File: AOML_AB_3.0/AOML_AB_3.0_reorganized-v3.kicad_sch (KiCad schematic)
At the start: 103 parts, among them IC11 SN74LVC1G3157DCKR, J1 Conn_01x04, J2 216550-1, J24 Conn_01x02, J3 Conn_01x03, J4 Conn_01x07, J5 Conn_01x03, J6 Conn_01x03, J7 Screw_Terminal_01x07, SW1 TS02-66-70-BK-160-LCR-D, U1 L7812ABD2T-TR, U2 LM7805MPX, U3 MCP1825ST-3302E/DB, U4 MAX3232, U5 INA213AIDCKR, U6 STM32F103RBTx, U7 AT24C01D-STUM-T, Y1 8MHz

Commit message: Board V3.0 rev3 completed: several footprints fixed, added mosfet inverter to GPS data input, buffer to Vin measurement, jumper to 12V motor supply bus, and made power rails wider
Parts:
- removed J6: Conn_01x03, Connector_PinHeader_2.54mm:PinHeader_1x03_P2.54mm_Vertical, symbol Connector_Generic:Conn_01x03
- removed JP10, JP11, JP9: SolderJumper_2_Open, Jumper:SolderJumper-2_P1.3mm_Open_RoundedPad1.0x1.5mm, symbol Jumper:SolderJumper_2_Open
- removed TP7: GND, TestPoint:TestPoint_Pad_1.0x1.0mm, symbol Connector:TestPoint
- added C78: 0.1u, Capacitor_01uF-0805:CAP_CL21_SAM, symbol Device:C
- added F1: 1A, Polyfuse_1A_1812:0ZCG_BEL, symbol Device:Polyfuse
- added J25: Conn_01x03, Connector_PinHeader_2.54mm:PinHeader_1x03_P2.54mm_Vertical, symbol Connector_Generic:Conn_01x03
- added J6: Conn_01x02, Connector_PinHeader_2.54mm:PinHeader_1x02_P2.54mm_Vertical, symbol Connector_Generic:Conn_01x02
- added Q1: BSS138, Mosfet_BSS138PW:SC-70_SOT323_NEX-M, symbol Transistor_FET:BSS138
- added R50: 10k, Resistor_0805:RC0805N_YAG, symbol Device:R_Small
- added U18: LMV321B-TR, OpAmp_LMV321B-TR:S5TSOT23-5-A_TPK-M, symbol Amplifier_Operational:LM321
- D4, D5, D6, D7: value green-led -> led
- H1, H2, H3, H4, H5, H6: footprint MountingHole:MountingHole_2.5mm_Pad -> MountingHole:MountingHole_6.4mm_M6_ISO7380_Pad
- R44: value 2k -> 2.4k; Digikey https://www.digikey.com/en/products/detail/yageo/RC0805FR-1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 -> https://www.digikey.com/en/products/detail/yageo/RC0805FR-0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; Part RC0805FR-132KL -> RC0805FR-072K4L
- R45: value 560 -> 750; Digikey https://www.digikey.com/en/products/detail/yageo/RC0805JR-0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 -> https://www.digikey.com/en/products/detail/yageo/RC0805FR-0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; Part RC0805JR-07560RL -> RC0805FR-07750RL
- R46, R47: value 220 -> 330; Digikey https://www.digikey.com/en/products/detail/yageo/RC0805FR-1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 -> https://www.digikey.com/en/products/detail/yageo/RC0805JR-0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; Part RC0805FR-13220RL -> RC0805JR-07330RL
- R48: value 6.8k -> 5.1k; Digikey https://www.digikey.com/en/products/detail/yageo/RT0805FRE076K8L/1079385 -> https://www.digikey.com/en/products/detail/yageo/RT0805FRE075K1L/1079334; Part RT0805FRE076K8L -> RT0805FRE075K1L
- R49: value 3.3k -> 10k; Digikey https://www.digikey.com/en/products/detail/yageo/RT0805FRE073K3L/1079226 -> https://www.digikey.com/en/products/detail/yageo/RT0805FRE0710KL/1078908; Part RT0805FRE073K3L -> RT0805FRE0710KL
- Y1: footprint Crystal_8MHZ_smt:XTAL_ABLS-8.000MHz-20-B-3-H-T -> Crystal_8mhz_small:XTAL_ABM3-8.000MHZ-D2Y-T_ABR-M; Cost 0.17 -> 0.57; Digikey https://www.digikey.com/en/products/detail/abracon-llc/ABLS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 -> https://www.digikey.com/en/products/detail/abracon-llc/ABM3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; Part ABLS-8.000MHZ-20-B-3-H-T -> ABM3-8.000MHZ-D2Y-T
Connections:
- net +12V: now also C2.1, U1.3 (VO), U2.1 (VI); no longer U1.2 (VO)
- net +19.5V: now also R3.2, U1.1 (VI); no longer C2.1, JP1.2 (B), U1.3 (VI), U2.3 (VI)
- net +3.3V: now also C26.1, C28.1, JP1.2 (B), U3.3 (VO), U5.3 (V+), U7.4 (VCC), R50.1, U18.5 (V+); no longer C11.1, C16.1, C21.1, C4.1, C6.1, C9.1, FB1.1, J1.1 (Pin_1), TP3.1, U3.2 (VO), U6.1 (VBAT), U6.19 (VDD), U6.32 (VDD), U6.48 (VDD), U6.64 (VDD)
- net +5V: now also U2.3 (VO), U3.1 (VI), F1.1; no longer J3.1 (Pin_1), U2.2 (VO), U3.3 (VI)
- net Din_fromGPS: now also Q1.3 (D), R50.2; no longer R48.1, R49.1
- net GND: now also R48.1, U1.2 (GND), U2.2 (GND), U3.2 (GND), U5.1 (REF), U7.5 (WP), C78.2, J25.3 (Pin_3), Q1.2 (S), U18.2 (V-); no longer R48.2, U1.1 (GND), U2.1 (GND), U3.1 (GND), U5.5 (REF)
- net Vmotor_out: now also J6.1 (Pin_1); no longer JP5.1 (A), R5.1
- net relay_xbt1: now also U6.52 (PC11); no longer U6.57 (PB5)
- net relay_xbt2: now also U6.53 (PC12); no longer U6.56 (PB4)
- net relay_xbt3: now also U6.54 (PD2); no longer U6.55 (PB3)
- net relay_xbt4: now also U6.55 (PB3); no longer U6.54 (PD2)
- net relay_xbt5: now also U6.56 (PB4); no longer U6.53 (PC12)
- net relay_xbt6: now also U6.57 (PB5); no longer U6.52 (PC11)
- net at JP5.2 (B): now also U5.5 (-); no longer U5.4 (-)
- net at D3.K, TP2.1, U6.9 (PC1): now also U5.6; no longer U5.1
- net at D2.K, TP1.1, U6.8 (PC0): now also U18.3 (-), U18.4; no longer R3.1, R4.1
- net at JP4.2 (B): now also U5.4 (+); no longer U5.3 (+)
- net at R6.1: now also J25.2 (Pin_2)
- net VDD: now reaches JP1.1 (A)
- net VDD: now also C11.1, C16.1, C21.1, C4.1, C6.1, C9.1, FB1.1, J1.1 (Pin_1), TP3.1, U6.1 (VBAT), U6.19 (VDD), U6.32 (VDD), U6.48 (VDD), U6.64 (VDD), J25.1 (Pin_1); no longer R3.2
- new net: C78.1, R3.1, R4.1, U18.1 (+)
- new net: J6.2 (Pin_2), JP5.1 (A), R5.1
- new net: Q1.1 (G), R48.2, R49.1
- new net: F1.2, J3.1 (Pin_1)
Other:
- note added: "3:1"
- note added: "Buffer G=1"
- note added: "Fcutoff ~30Hz -> 30ms"
- note added: "GPS manual"
- note added: "Garmin GPS 18x LVC: 90 mA @ 5.0 Vdc RS232: -5.5V (1) / +5.5V (0) TTL: +3.3V (1) / 0V (0)"
- note added: "I hold = 0.5A I trip = 1A"
- note added: "Open JP1 when powered from ST-Link"
- note added: "Open jumper when uploading firmware and motors are connected. Enable pins are active low and all motors are powered"
- note added: "REV 3 changes: -Several footprints had wrong pinout in 1st version. Footprints corrected: linear regulator 5V, 12V, 3V3, INA213. -GPS DataIn is buffered with mosfet to change -5/+5 levels to TTL 3V3 -Copper fill was added for heat dissipation on DRV8825 and voltage regulators -Mounting holes were enlarge to original V2.3 board size -Min track and clearances was changed to 0.2 mm -Power tracks are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"
- note removed: "Garmin GPS 18x LVC: 90 mA @ 5.0 Vdc CMOS Serial Output Levels: GPS 18x LVC and GPS 18x-5Hz: 0 Vdc to Vin between 4 and 5.5 Vdc (Asynchronous Serial, TIA-232-F (RS-232) Compatible Polarity)"
- note removed: "TTL Input: 0<V<0.8 LOW 2<V<5 HIGH"
- moved on the sheet: C10, C11, C16, C4, C6, C7, C9, FB1, J3, R3, R4, R48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

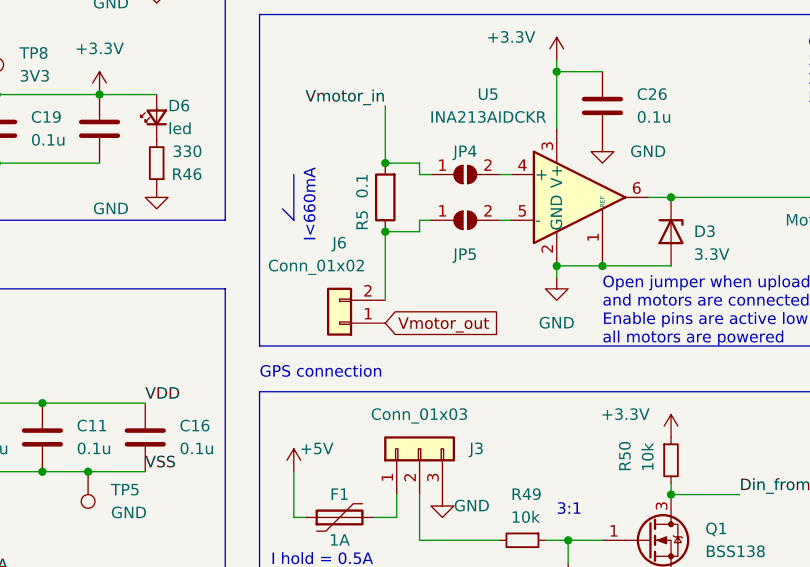
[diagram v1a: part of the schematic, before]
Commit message: rev3 completed with thermal relief fixes and linear reg GND copper fills expanded, LCD I2C tested ok, DRV8825 control changed to sleep pin to avoid startup coil
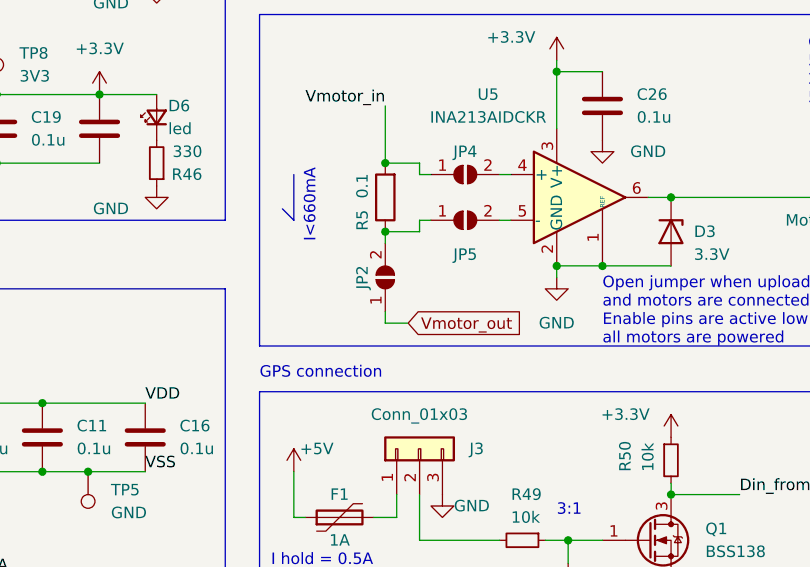
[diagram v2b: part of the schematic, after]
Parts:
- removed J6: Conn_01x02, Connector_PinHeader_2.54mm:PinHeader_1x02_P2.54mm_Vertical, symbol Connector_Generic:Conn_01x02
- added JP2: SolderJumper_2_Open, Jumper:SolderJumper-2_P1.3mm_Open_RoundedPad1.0x1.5mm, symbol Jumper:SolderJumper_2_Open
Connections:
- net Vmotor_out: now also JP2.1 (A)
- net at JP5.1 (A), R5.1: now also JP2.2 (B)
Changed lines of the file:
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@@
   (junction (at 147.32 113.03) (diameter 0) (color 0 0 0 0)
   )
-  (junction (at 311.15 125.73) (diameter 0) (color 0 0 0 0)
-  )
   (junction (at 95.25 116.84) (diameter 0) (color 0 0 0 0)
   )
+  (junction (at 311.15 125.73) (diameter 0) (color 0 0 0 0)
+  )
   (junction (at 57.15 135.89) (diameter 0) (color 0 0 0 0)
   )
@@
     (stroke (width 0) (type default))
   )
+  (wire (pts (xy 95.25 125.73) (xy 95.25 127))
+    (stroke (width 0) (type default))
+  )
   (wire (pts (xy 52.07 55.88) (xy 63.5 55.88))
     (stroke (width 0) (type default))
@@
     (stroke (width 0) (type default))
   )
+  (wire (pts (xy 97.79 127) (xy 95.25 127))
+    (stroke (width 0) (type default))
+  )
   (wire (pts (xy 146.05 254) (xy 153.67 254))
     (stroke (width 0) (type default))
@@
     (stroke (width 0) (type default))
   )
+  (wire (pts (xy 95.25 118.11) (xy 95.25 116.84))
+    (stroke (width 0) (type default))
+  )
   (wire (pts (xy 158.75 71.12) (xy 158.75 113.03))
     (stroke (width 0) (type default))
@@
     (stroke (width 0) (type default))
   )
-  (wire (pts (xy 95.25 116.84) (xy 95.25 124.46))
-    (stroke (width 0) (type default))
-  )
   (wire (pts (xy 17.78 55.88) (xy 29.21 55.88))
     (stroke (width 0) (type default))
@@
     )
   )
-  (global_label "Vmotor_out" (shape input) (at 95.25 127 0) (fields_autoplaced)
+  (global_label "Vmotor_out" (shape input) (at 97.79 127 0) (fields_autoplaced)
     (effects (font (size 1.27 1.27)) (justify left))
-    (property "Intersheetrefs" "${INTERSHEET_REFS}" (at 108.8183 127 0)
+    (property "Intersheetrefs" "${INTERSHEET_REFS}" (at 111.3583 127 0)
       (effects (font (size 1.27 1.27)) (justify left) hide)
     )
@@
     )
   )
-  (symbol (lib_id "Connector_Generic:Conn_01x02") (at 90.17 127 180) (unit 1)
-    (in_bom yes) (on_board yes) (dnp no)
-    (property "Reference" "J6" (at 90.17 118.11 0)
-      (effects (font (size 1.27 1.27)))
-    )
-    (property "Value" "Conn_01x02" (at 87.63 120.65 0)
-      (effects (font (size 1.27 1.27)))
-    )
-    (property "Footprint" "Connector_PinHeader_2.54mm:PinHeader_1x02_P2.54mm_Vertical" (at 90.17 127 0)
-      (effects (font (size 1.27 1.27)) hide)
-    )
-    (property "Datasheet" "https://www.we-online.com/components/products/datasheet/61300211121.pdf" (at 90.17 127 0)
-      (effects (font (size 1.27 1.27)) hide)
-    )
-    (property "Digikey" "https://www.digikey.com/en/products/detail/w%C3%BCrth-elektronik/61300211121/4846823" (at 90.17 127 0)
-      (effects (font (size 1.27 1.27)) hide)
-    )
-    (property "Cost" "0.13" (at 90.17 127 0)
-      (effects (font (size 1.27 1.27)) hide)
-    )
-    (property "Part" "61300211121" (at 90.17 127 0)
-      (effects (font (size 1.27 1.27)) hide)
-    )
-    (pin "1")
-    (pin "2")
-    (instances
-      (project "AOML_AB_3.0_reorganized-v3"
-        (path "/6a222f58-627e-41ff-951d-9ad8d2e0d7a2"
-          (reference "J6") (unit 1)
-        )
-      )
-    )
-  )
   (symbol (lib_id "Device:C") (at 105.41 34.29 0) (unit 1)
     (in_bom yes) (on_board yes) (dnp no) (fields_autoplaced)
@@
         )
       )
+    )
+  )
+  (symbol (lib_id "Jumper:SolderJumper_2_Open") (at 95.25 121.92 90) (unit 1)
+    (in_bom yes) (on_board yes) (dnp no)
+    (property "Reference" "JP2" (at 92.71 121.92 0)
+      (effects (font (size 1.27 1.27)))
+    )
+    (property "Value" "SolderJumper_2_Open" (at 91.44 121.92 0)
+      (effects (font (size 1.27 1.27)) hide)
+    )
+    (property "Footprint" "Jumper:SolderJumper-2_P1.3mm_Open_RoundedPad1.0x1.5mm" (at 95.25 121.92 0)
+      (effects (font (size 1.27 1.27)) hide)
+    )
+    (property "Datasheet" "~" (at 95.25 121.92 0)
+      (effects (font (size 1.27 1.27)) hide)
+    )
+    (property "Cost" "" (at 95.25 121.92 0)
+      (effects (font (size 1.27 1.27)) hide)
+    )
+    (property "Part" "" (at 95.25 121.92 0)
+      (effects (font (size 1.27 1.27)) hide)
+    )
+    (pin "1")
+    (pin "2")
+    (instances
+      (project "AOML_AB_3.0_reorganized-v3"
+        (path "/6a222f58-627e-41ff-951d-9ad8d2e0d7a2"
+          (reference "JP2") (unit 1)
+        )
+      )

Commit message: Rewired main RJ45 matching previous V2.3 connector and replaced 1000uF capacitor for THT. PCB v3 rev3 ready to manufacture, BOM and gerbers generated
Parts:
- C5: footprint Capacitor_1000uF_can-smt:CAP_EEV_H13_PAN -> Capacitor_THT1000uF:CAP_PK&slash_PZ_10X16_LOW_RUB; Cost 1.23 -> 0.67; Digikey https://www.digikey.com/en/products/detail/panasonic-electr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 -> https://www.digikey.com/en/products/detail/rubycon/25PX1000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; Part EEV-FK1E102Q -> 25PX1000MEFCT810X16
- renumbered JP13 to JP12, JP12 to JP13
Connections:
- net +19.5V_raw: now also J2.4, J2.5; no longer J2.2, J2.6
- net Din_fromComputer: now also J2.3; no longer J2.7
- net Dout_toComputer: now also J2.6; no longer J2.3
- net GND: now also J2.8; no longer J2.4
- net xbt_A: now also JP12.2 (B); no longer JP13.2 (B)
- net xbt_B: now also JP13.2 (B); no longer JP12.2 (B)
- net at JP13.1 (A): now also J2.2; no longer J2.8
- net at JP14.1 (A): now also J2.7; no longer J2.5
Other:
- note added: "PC-Rx (RS-232) <- uC||gps Tx"
- note added: "PC-Tx (RS-232) -> uC-Rx"
- note removed: "Rx RS-232 <-"
- note removed: "Tx RS-232 ->"
- moved on the sheet: J24, J5, JP12, JP13, JP14

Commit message: Board V3.0 rev3 without changes since last commit, old versions cleanup in directory
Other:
- note added: "replaced by MAX3232IPWR"
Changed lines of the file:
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@@
+    (effects (font (size 1.27 1.27)) (justify left bottom))
+  )
+  (text "replaced by MAX3232IPWR" (at 93.98 274.32 0)
     (effects (font (size 1.27 1.27)) (justify left bottom))
   )
